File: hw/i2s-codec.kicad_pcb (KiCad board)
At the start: 2 copper layers, 1 part, among them IC1 TAC5212IRGER

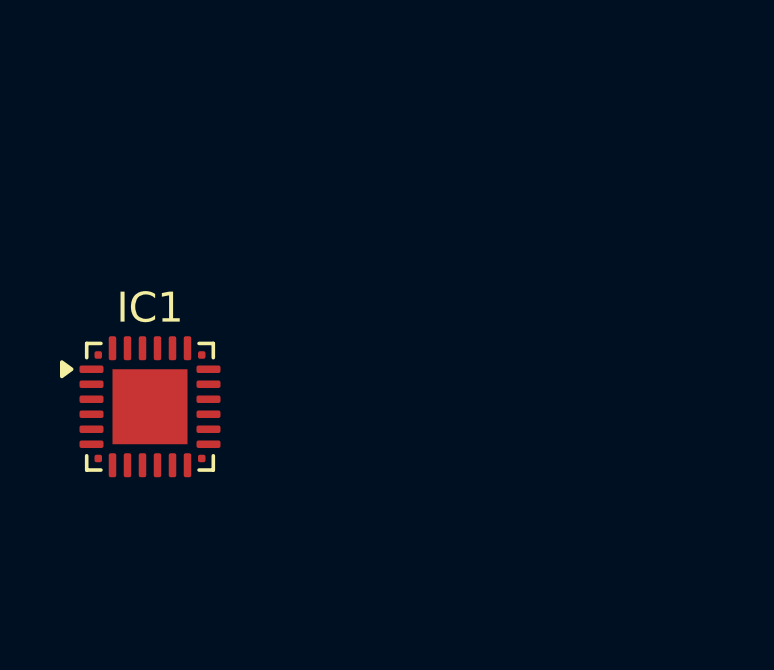
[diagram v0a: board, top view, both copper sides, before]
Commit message: Schematic now has electret mic, exposes most connections to the IC and conditions the output lines
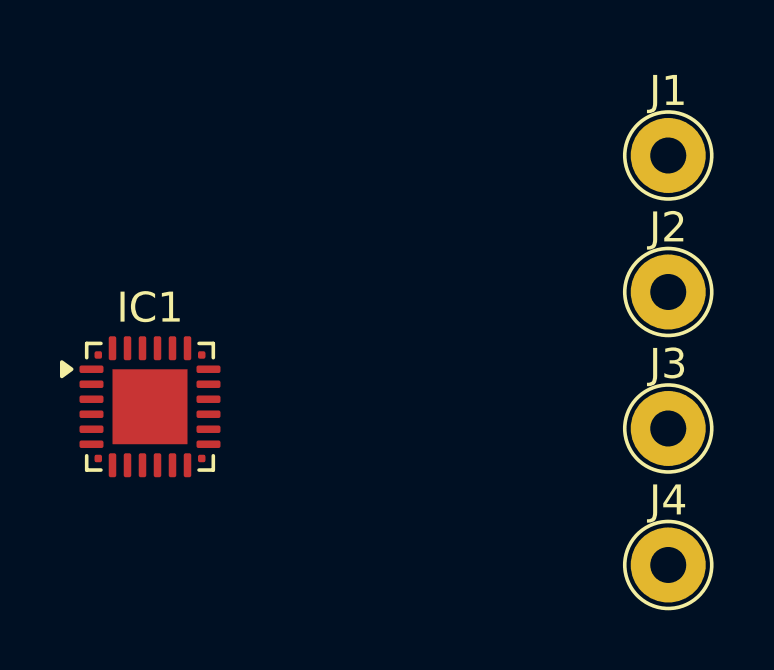
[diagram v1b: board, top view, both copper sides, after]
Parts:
- added J1: Conn_01x01_Pin, TestPoint:TestPoint_THTPad_D2.5mm_Drill1.2mm, F.Cu at (165.5, 89.8)
- added J2: Conn_01x01_Pin, TestPoint:TestPoint_THTPad_D2.5mm_Drill1.2mm, F.Cu at (165.5, 94.4)
- added J3: Conn_01x01_Pin, TestPoint:TestPoint_THTPad_D2.5mm_Drill1.2mm, F.Cu at (165.5, 99.0)
- added J4: Conn_01x01_Pin, TestPoint:TestPoint_THTPad_D2.5mm_Drill1.2mm, F.Cu at (165.5, 103.5)
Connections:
- IC1 pad 1: unconnected-(IC1-DREG-Pad1) -> Net-(IC1-DREG)
- IC1 pad 14: unconnected-(IC1-MICBIAS-Pad14) -> /MICBIAS
- IC1 pad 19: unconnected-(IC1-OUT1M-Pad19) -> /OUT1M
- IC1 pad 20: unconnected-(IC1-OUT1P-Pad20) -> /OUT1P
- IC1 pad 21: unconnected-(IC1-OUT2P-Pad21) -> /OUT2P
- IC1 pad 22: unconnected-(IC1-OUT2M-Pad22) -> /OUT2M
- IC1 pad 23: unconnected-(IC1-AVDD-Pad23) -> Net-(IC1-AVDD)
- IC1 pad 24: unconnected-(IC1-VREF-Pad24) -> Net-(IC1-VREF)
- IC1 pad 25: unconnected-(IC1-VSS_1-Pad25) -> GND
- IC1 pad 6: unconnected-(IC1-IOVDD-Pad6) -> Net-(IC1-IOVDD)
- IC1 pad A1: unconnected-(IC1-VSS_2-PadA1) -> GND
- IC1 pad A2: unconnected-(IC1-VSS_3-PadA2) -> GND
- IC1 pad A3: unconnected-(IC1-VSS_4-PadA3) -> GND
- IC1 pad A4: unconnected-(IC1-VSS_5-PadA4) -> GND
